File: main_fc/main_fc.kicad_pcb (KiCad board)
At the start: 2 copper layers, 198 parts, among them U1 ADS1158IRTCR, U10 AD8495, U11 AD8495, U12 AD8495, U13 AD8495, U14 AD8495, U15 AD8495, U2 AD8495, U3 OP777ARZ, U4 STM32H730ZBTx, U6 LAN8742A, U7 FT232RL, U8 ADS1158IRTCR, U9 AD8495

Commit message: updated TC routing
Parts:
- moved R10 78.8 mm to (39.2, 35.3)
- moved R11 78.8 mm to (42.2, 35.3)
- moved R12 75.8 mm to (52.1, 34.5), turned to 180 degrees
- moved U2 72.3 mm to (47.4, 37.9)
- moved C14 71.6 mm to (42.9, 39.1), turned to 90 degrees
- moved C12 71.0 mm to (52.1, 37.6), turned to 180 degrees
- moved C13 70.9 mm to (41.4, 39.1), turned to -90 degrees
- moved C8 69.3 mm to (42.2, 36.8), turned to 180 degrees
- moved C9 69.3 mm to (47.3, 35.3), turned to 180 degrees
- moved C10 68.0 mm to (52.1, 36.1), turned to 180 degrees
- moved C11 67.6 mm to (52.1, 39.1), turned to 180 degrees
- moved R50 61.7 mm to (52.2, 42.4), turned to 180 degrees
- moved R49 59.5 mm to (42.3, 43.2)
- moved C75 58.7 mm to (52.2, 45.5), turned to 180 degrees
- moved C1 58.5 mm to (80.2, 83.3)
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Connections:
- net /TC/+ renamed /TC0/TC_INPUT+
- net /TC/- renamed /TC0/TC_INPUT-
- net /TC/TC_OUT renamed /TC0/TC_OUT
- net /TC1/+ renamed /TC1/TC_INPUT+
- net /TC1/- renamed /TC1/TC_INPUT-
- net /TC2/+ renamed /TC2/TC_INPUT+
- net /TC2/- renamed /TC2/TC_INPUT-
- net /TC3/+ renamed /TC3/TC_INPUT+
- net /TC3/- renamed /TC3/TC_INPUT-
- net /TC4/+ renamed /TC4/TC_INPUT+
- net /TC4/- renamed /TC4/TC_INPUT-
- net /TC5/+ renamed /TC5/TC_INPUT+
- net /TC5/- renamed /TC5/TC_INPUT-
- net /TC6/+ renamed /TC6/TC_INPUT+
- net /TC6/- renamed /TC6/TC_INPUT-
- net /TC7/+ renamed /TC7/TC_INPUT+
- net /TC7/- renamed /TC7/TC_INPUT-
- U1 pad 1: unconnected-(U1-AIN3-Pad1) -> /ADC0/AIN3
- U1 pad 2: unconnected-(U1-AIN2-Pad2) -> /ADC0/AIN2
- U1 pad 3: unconnected-(U1-AIN1-Pad3) -> /ADC0/AIN1
- U1 pad 33: unconnected-(U1-AIN15-Pad33) -> /ADC0/AIN15
- U1 pad 34: unconnected-(U1-AIN14-Pad34) -> /ADC0/AIN14
- U1 pad 35: unconnected-(U1-AIN13-Pad35) -> /ADC0/AIN13
- U1 pad 36: unconnected-(U1-AIN12-Pad36) -> /ADC0/AIN12
- U1 pad 37: unconnected-(U1-AIN11-Pad37) -> /ADC0/AIN11
- U1 pad 38: unconnected-(U1-AIN10-Pad38) -> /ADC0/AIN10
- U1 pad 39: unconnected-(U1-AIN9-Pad39) -> /ADC0/AIN9
- U1 pad 4: TC_CHIP_OUT -> /ADC0/AIN0
- U1 pad 40: unconnected-(U1-AIN8-Pad40) -> /ADC0/AIN8
- U1 pad 45: unconnected-(U1-AIN7-Pad45) -> /ADC0/AIN7
- U1 pad 46: unconnected-(U1-AIN6-Pad46) -> /ADC0/AIN6
- U1 pad 47: unconnected-(U1-AIN5-Pad47) -> /ADC0/AIN5
- U1 pad 48: unconnected-(U1-AIN4-Pad48) -> /ADC0/AIN4
- U8 pad 1: unconnected-(U8-AIN3-Pad1) -> /ADC1/AIN3
- U8 pad 2: unconnected-(U8-AIN2-Pad2) -> /ADC1/AIN2
- U8 pad 3: unconnected-(U8-AIN1-Pad3) -> /ADC1/AIN1
- U8 pad 33: unconnected-(U8-AIN15-Pad33) -> /ADC1/AIN15
- U8 pad 34: unconnected-(U8-AIN14-Pad34) -> /ADC1/AIN14
- U8 pad 35: unconnected-(U8-AIN13-Pad35) -> /ADC1/AIN13
- U8 pad 36: unconnected-(U8-AIN12-Pad36) -> /ADC1/AIN12
- U8 pad 37: unconnected-(U8-AIN11-Pad37) -> /ADC1/AIN11
- U8 pad 38: unconnected-(U8-AIN10-Pad38) -> /ADC1/AIN10
- U8 pad 39: unconnected-(U8-AIN9-Pad39) -> /ADC1/AIN9
- U8 pad 4: TC_CHIP_OUT -> /ADC1/AIN0
- U8 pad 40: unconnected-(U8-AIN8-Pad40) -> /ADC1/AIN8
- U8 pad 45: unconnected-(U8-AIN7-Pad45) -> /ADC1/AIN7
- U8 pad 46: unconnected-(U8-AIN6-Pad46) -> /ADC1/AIN6
- U8 pad 47: unconnected-(U8-AIN5-Pad47) -> /ADC1/AIN5
- U8 pad 48: unconnected-(U8-AIN4-Pad48) -> /ADC1/AIN4
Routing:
- added copper zone on B.Cu, net GND
- added copper zone on F.Cu, net GND

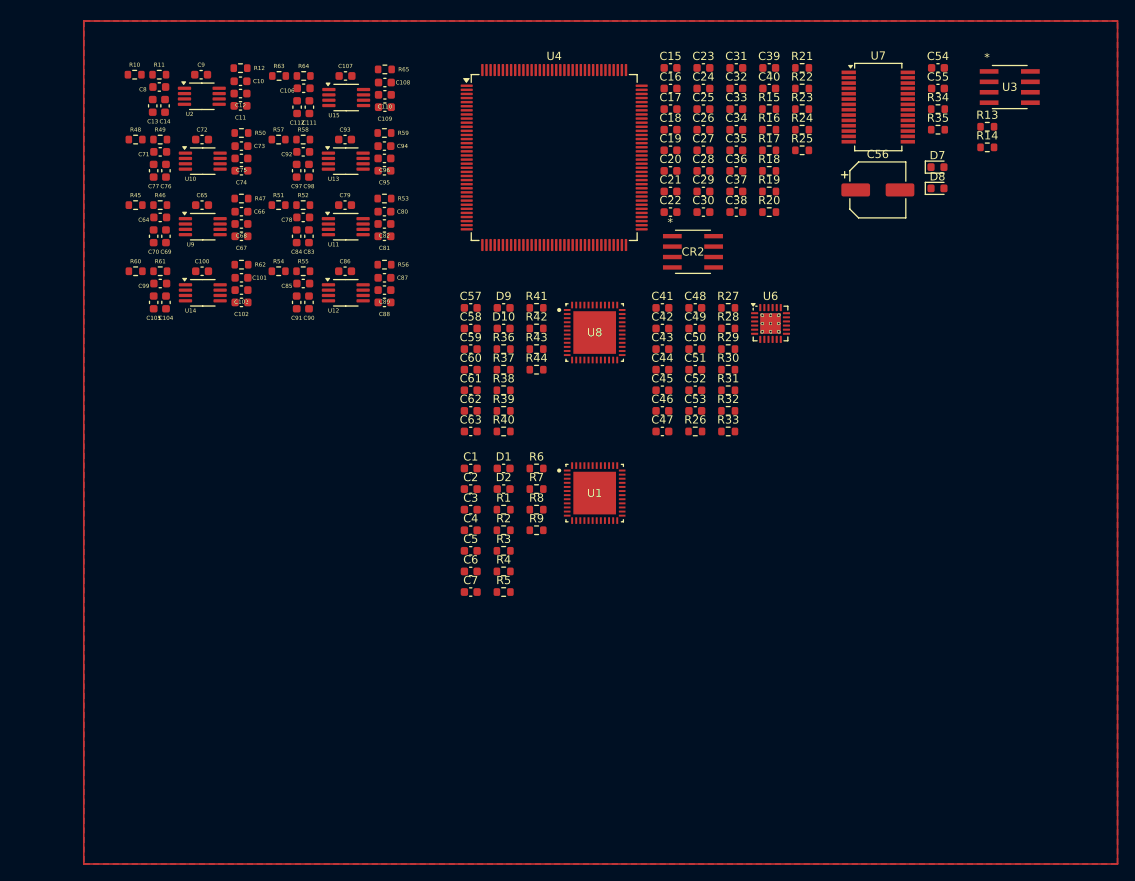
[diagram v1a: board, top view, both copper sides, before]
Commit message: sized main flight computer at 100mm x 100mm initially
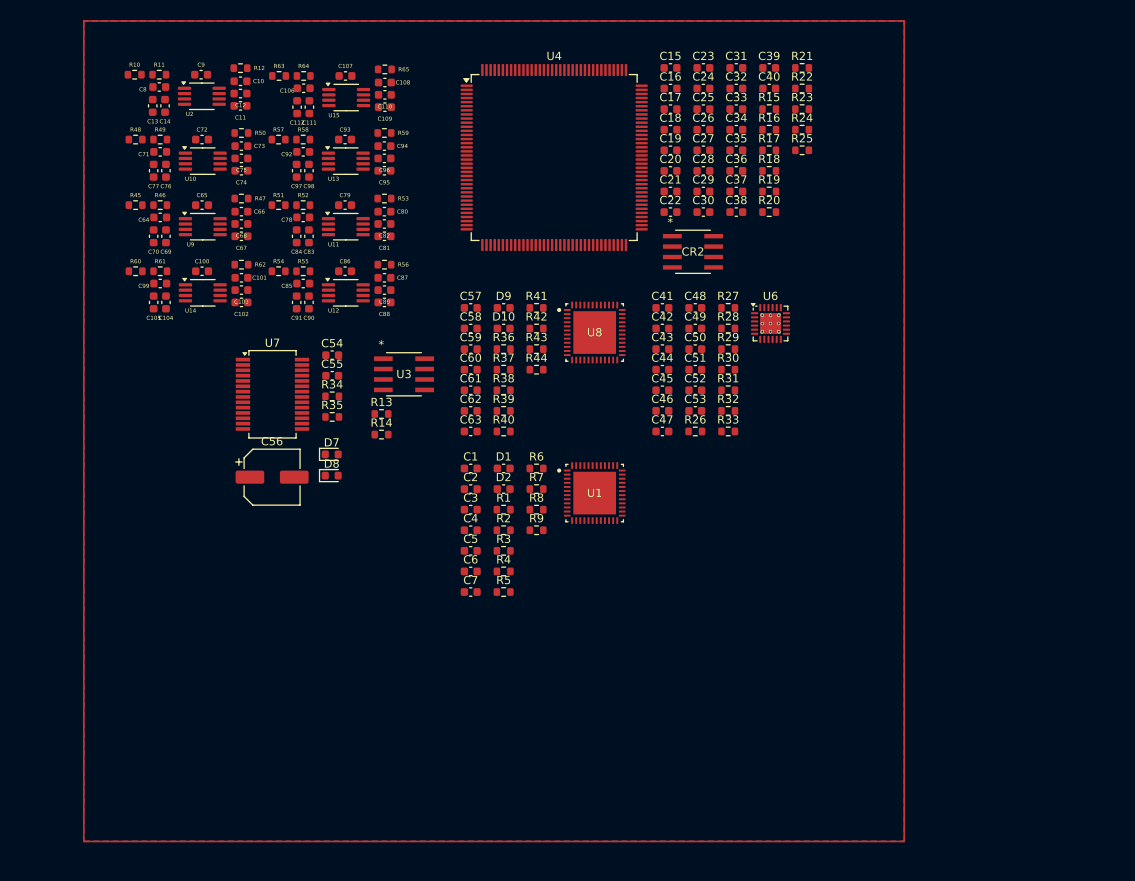
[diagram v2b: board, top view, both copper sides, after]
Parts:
- moved C54 81.7 mm to (63.3, 69.5)
- moved C55 81.7 mm to (63.3, 72.0)
- moved D7 81.7 mm to (63.2, 81.6)
- moved D8 81.7 mm to (63.2, 84.2)
- moved R34 81.7 mm to (63.3, 74.5)
- moved R35 81.7 mm to (63.3, 77.0)
- moved U7 81.7 mm to (56.0, 74.2)
- moved C56 81.7 mm to (56.0, 84.3)
- moved R13 81.7 mm to (69.3, 76.7)
- moved R14 81.7 mm to (69.3, 79.2)
- moved U3 81.7 mm to (72.0, 71.8)
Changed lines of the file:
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@@
 	(footprint "Capacitor_SMD:C_0603_1608Metric"
 		(layer "F.Cu")
-		(at 137.115 34.47)
+		(at 63.28 69.48)
 		(descr "Capacitor SMD 0603 (1608 Metric), square (rectangular) end terminal, IPC-7351 nominal, (Body size source: IPC-SM-782 page 76, https://www.pcb-3d.com/wordpress/wp-content/uploads/ipc-sm-782a_amendment_1_and_2.pdf), generated with kicad-footprint-generator")
 		(tags "capacitor")
@@
 	(footprint "Resistor_SMD:R_0603_1608Metric"
 		(layer "F.Cu")
-		(at 137.115 42)
+		(at 63.28 77.01)
 		(descr "Resistor SMD 0603 (1608 Metric), square (rectangular) end terminal, IPC-7351 nominal, (Body size source: IPC-SM-782 page 72, https://www.pcb-3d.com/wordpress/wp-content/uploads/ipc-sm-782a_amendment_1_and_2.pdf), generated with kicad-footprint-generator")
 		(tags "resistor")
@@
 	(footprint "Capacitor_SMD:C_0603_1608Metric"
 		(layer "F.Cu")
-		(at 137.115 36.98)
+		(at 63.28 71.99)
 		(descr "Capacitor SMD 0603 (1608 Metric), square (rectangular) end terminal, IPC-7351 nominal, (Body size source: IPC-SM-782 page 76, https://www.pcb-3d.com/wordpress/wp-content/uploads/ipc-sm-782a_amendment_1_and_2.pdf), generated with kicad-footprint-generator")
 		(tags "capacitor")
@@
 	(footprint "Capacitor_SMD:CP_Elec_6.3x7.7"
 		(layer "F.Cu")
-		(at 129.785 49.34)
+		(at 55.95 84.35)
 		(descr "SMD capacitor, aluminum electrolytic, Nichicon, 6.3x7.7mm")
 		(tags "capacitor electrolytic")
@@
 	(footprint "Resistor_SMD:R_0603_1608Metric"
 		(layer "F.Cu")
-		(at 143.125 44.15)
+		(at 69.29 79.16)
 		(descr "Resistor SMD 0603 (1608 Metric), square (rectangular) end terminal, IPC-7351 nominal, (Body size source: IPC-SM-782 page 72, https://www.pcb-3d.com/wordpress/wp-content/uploads/ipc-sm-782a_amendment_1_and_2.pdf), generated with kicad-footprint-generator")
 		(tags "resistor")
@@
 	(footprint "LED_SMD:LED_0603_1608Metric"
 		(layer "F.Cu")
-		(at 137.055 49.15)
+		(at 63.22 84.16)
 		(descr "LED SMD 0603 (1608 Metric), square (rectangular) end terminal, IPC-7351 nominal, (Body size source: http://www.tortai-tech.com/upload/download/2011102023233369053.pdf), generated with kicad-footprint-generator")
 		(tags "LED")
@@
 	(footprint "Package_SO:SSOP-28_5.3x10.2mm_P0.65mm"
 		(layer "F.Cu")
-		(at 129.835 39.24)
+		(at 56 74.25)
 		(descr "28-Lead Plastic Shrink Small Outline (SS)-5.30 mm Body [SSOP] (see Microchip Packaging Specification 00000049BS.pdf)")
 		(tags "SSOP 0.65")
@@
 	(footprint "avi_footprint:R_8_ADI-M"
 		(layer "F.Cu")
-		(at 145.8618 36.8011)
+		(at 72.0268 71.8111)
 		(tags "OP777ARZ ")
 		(property "Reference" "U3"
@@
 	(footprint "Resistor_SMD:R_0603_1608Metric"
 		(layer "F.Cu")
-		(at 137.115 39.49)
+		(at 63.28 74.5)
 		(descr "Resistor SMD 0603 (1608 Metric), square (rectangular) end terminal, IPC-7351 nominal, (Body size source: IPC-SM-782 page 72, https://www.pcb-3d.com/wordpress/wp-content/uploads/ipc-sm-782a_amendment_1_and_2.pdf), generated with kicad-footprint-generator")
 		(tags "resistor")
@@
 	(footprint "Resistor_SMD:R_0603_1608Metric"
 		(layer "F.Cu")
-		(at 143.125 41.64)
+		(at 69.29 76.65)
 		(descr "Resistor SMD 0603 (1608 Metric), square (rectangular) end terminal, IPC-7351 nominal, (Body size source: IPC-SM-782 page 72, https://www.pcb-3d.com/wordpress/wp-content/uploads/ipc-sm-782a_amendment_1_and_2.pdf), generated with kicad-footprint-generator")
 		(tags "resistor")
@@
 	(footprint "LED_SMD:LED_0603_1608Metric"
 		(layer "F.Cu")
-		(at 137.055 46.56)
+		(at 63.22 81.57)
 		(descr "LED SMD 0603 (1608 Metric), square (rectangular) end terminal, IPC-7351 nominal, (Body size source: http://www.tortai-tech.com/upload/download/2011102023233369053.pdf), generated with kicad-footprint-generator")
 		(tags "LED")
@@
 	(gr_rect
 		(start 33 28.75)
-		(end 159 131.5)
+		(end 133 128.75)
 		(stroke
 			(width 0.2)
-			(type default)
+			(type solid)
 		)
 		(fill no)
@@
 	)
 	(zone
-		(net 2)
-		(net_name "GND")
-		(layers "F.Cu" "B.Cu")
-		(hatch edge 0.5)
-		(connect_pads
-			(clearance 0)
-		)
-		(min_thickness 0.25)
-		(filled_areas_thickness no)
-		(fill yes
-			(thermal_gap 0.5)
-			(thermal_bridge_width 0.5)
-		)
-		(polygon
-			(pts
-				(xy 159 28.75) (xy 33 28.75) (xy 33 131.5) (xy 159 131.5)
-			)
-		)
-	)
-	(zone
 		(net 0)
 		(net_name "")
@@
 			)
 		)
+	)
+	(zone
+		(net 2)
+		(net_name "GND")
+		(layers "F.Cu" "B.Cu")
+		(hatch edge 0.5)
+		(connect_pads
+			(clearance 0)
+		)
+		(min_thickness 0.25)
+		(filled_areas_thickness no)
+		(fill yes
+			(thermal_gap 0.5)
+			(thermal_bridge_width 0.5)
+		)
+		(polygon
+			(pts
+				(xy 133 28.75) (xy 33 28.75) (xy 33 128.75) (xy 133 128.75)
+			)
+		)
